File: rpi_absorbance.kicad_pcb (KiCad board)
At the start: 2 copper layers, 39 parts, among them CON1 BARREL_JACK, P1 DEVICE_CONN, P3 RPI_HEADER, P4 STEPPER_CONN, P5 SWITCH_CONN, Q1 NPN, U1 R-78B5.0-1.5L, U2 MEE1S1212SC, U3 DRV8825, U4 TCA9406DCUR

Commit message: Revise circuit
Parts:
- C13: footprint Capacitors_SMD:c_elec_8x6.7 -> Capacitors_SMD:C_1206
- moved Q1 41.0 mm to (157.2, 119.1)
- moved U2 39.8 mm to (155.4, 114.2)
- moved C7 14.6 mm to (112.5, 116.3)
- moved C10 14.6 mm to (115.7, 102.6)
- moved C14 14.6 mm to (115.7, 102.6)
- moved C15 14.6 mm to (115.7, 102.6)
- moved C16 14.6 mm to (115.7, 102.6)
- moved C17 14.6 mm to (115.7, 102.6)
- moved C18 14.6 mm to (115.7, 102.6)
- moved C4 14.6 mm to (107.2, 119.2)
- moved C8 14.6 mm to (115.7, 102.6)
- moved C9 14.6 mm to (115.7, 102.6)
- moved R10 14.6 mm to (115.7, 102.6)
- moved R2 14.6 mm to (115.7, 102.6)
- moved R3 14.6 mm to (115.7, 102.6)
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
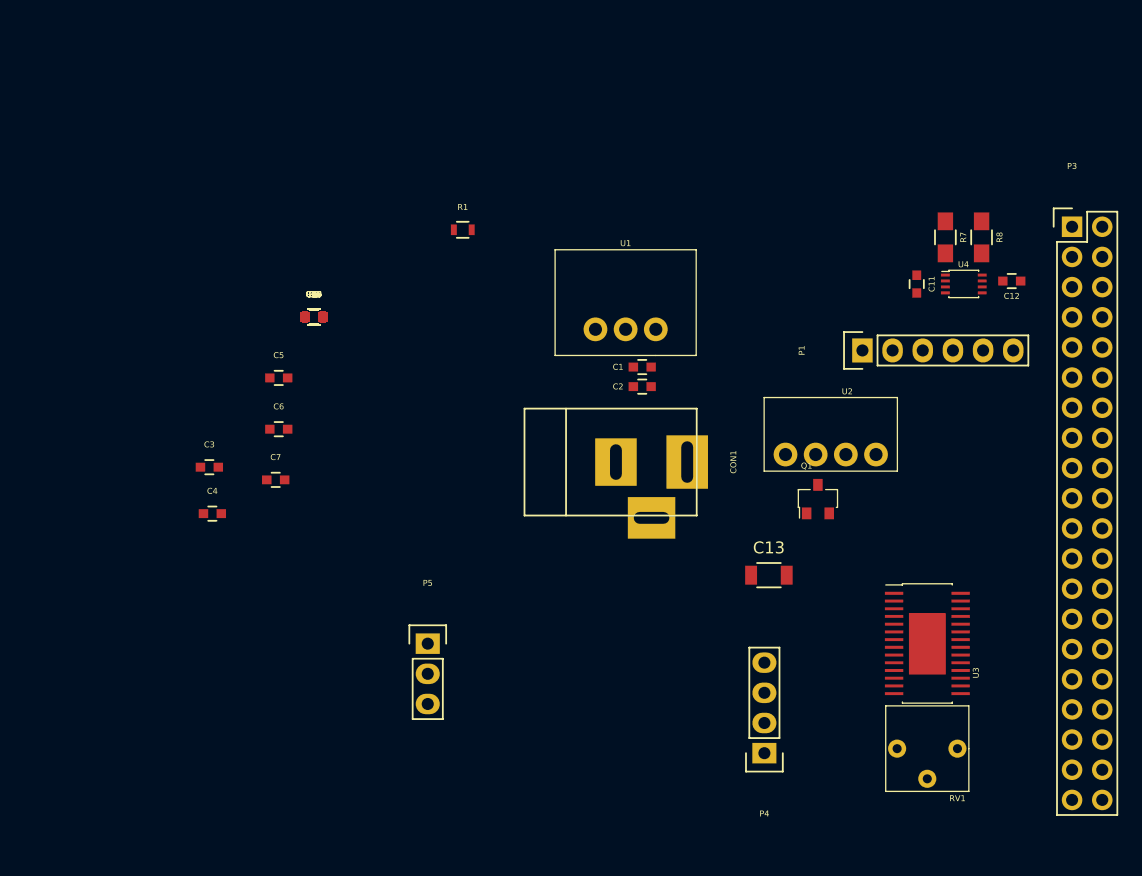
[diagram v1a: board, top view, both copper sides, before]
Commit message: Update footprints
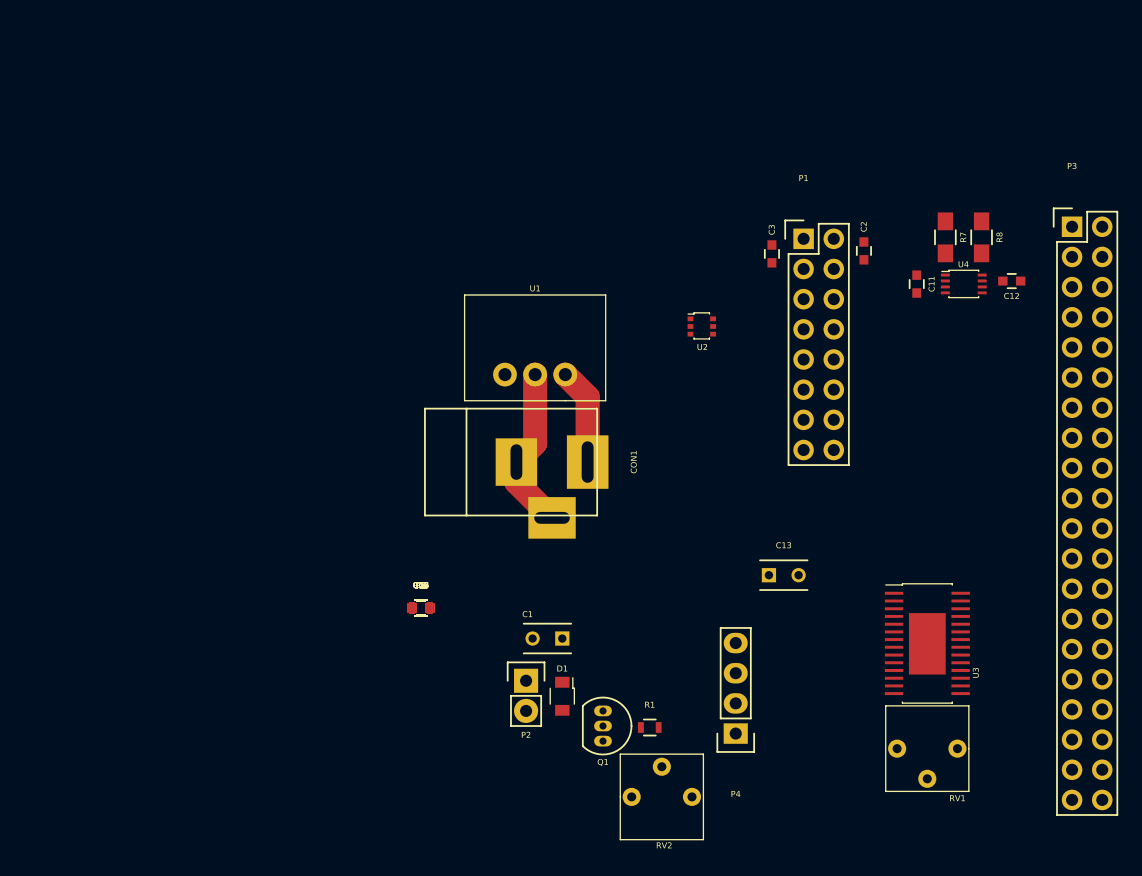
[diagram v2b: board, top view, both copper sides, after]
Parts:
- removed C10, C7, C8, C9: .1u, Capacitors_SMD:C_0603
- removed C4, C5, C6: 10u, Capacitors_SMD:C_0603
- removed P5: SWITCH_CONN, Pin_Headers:Pin_Header_Straight_1x03
- added D1: D, footprints:SOD-123, F.Cu at (136.7, 133.3)
- added P2: CONN_01X02, Pin_Headers:Pin_Header_Straight_1x02, F.Cu at (133.6, 133.2)
- added RV2: POT, footprints:BOURNS_3362P, F.Cu at (142.5, 143.0)
- C1: value .1u -> 100u; footprint Capacitors_SMD:C_0603 -> Capacitors_ThroughHole:C_Rect_L4_W2.5_P2.5
- C13: footprint Capacitors_SMD:C_1206 -> Capacitors_ThroughHole:C_Rect_L4_W2.5_P2.5
- P1: value DEVICE_CONN -> CONN_02X08; footprint Pin_Headers:Pin_Header_Straight_1x06 -> Pin_Headers:Pin_Header_Straight_2x08
- Q1: value NPN -> ZTX692B; footprint footprints:3-CP -> TO_SOT_Packages_THT:TO-92_Inline_Narrow_Oval
- R1: value 500 -> 1k
- U2: value MEE1S1212SC -> MUN5216DW1T1G; footprint footprints:MEE1-4-SIP -> footprints:SOT−363
- moved C3 50.7 mm to (154.3, 97.3), turned to 270 degrees
- moved R1 44.8 mm to (144.0, 137.2)
- moved C14 26.1 mm to (124.8, 127.1)
- moved C15 26.1 mm to (124.8, 127.1)
- moved C16 26.1 mm to (124.8, 127.1)
- moved C17 26.1 mm to (124.8, 127.1)
- moved C18 26.1 mm to (124.8, 127.1)
- moved R10 26.1 mm to (124.8, 127.1)
- moved R2 26.1 mm to (124.8, 127.1)
- moved R3 26.1 mm to (124.8, 127.1)
- moved R4 26.1 mm to (124.8, 127.1)
- moved R5 26.1 mm to (124.8, 127.1)
- moved R6 26.1 mm to (124.8, 127.1)
- moved R9 26.1 mm to (124.8, 127.1)
- moved Q1 23.9 mm to (140.1, 135.8), turned to 270 degrees
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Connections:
- C2 pad 1: +12V -> +5V
- C3 pad 1: +12V -> GND
- C3 pad 2: GND -> +12V
- CON1 pad 3: (no net) -> GND
- P1 pad 2: +5V -> GND
- P1 pad 3: /5vSDA -> +12V
- P1 pad 4: /5vSCL -> +5V
- P1 pad 5: /ISO-0v -> Net-(P1-Pad5)
- P1 pad 6: /ISO-12v -> /5vSDA
- P3 pad 11: /MODE2 -> /LED2
- P3 pad 13: /MODE1 -> /SWITCH1
- P3 pad 15: /MODE0 -> /SWITCH2
- P3 pad 19: /STEP -> /GPIO10
- P3 pad 21: /nENBL -> /GPIO9
- P3 pad 23: /DIR -> /GPIO11
- P3 pad 24: (no net) -> /PERI
- P3 pad 26: (no net) -> /nSLEEP
- P3 pad 29: /DECAY -> /MODE2
- P3 pad 31: /nFAULT -> /MODE1
- P3 pad 32: (no net) -> /nRESET
- P3 pad 33: /nSLEEP -> /MODE0
- P3 pad 35: /nRESET -> /STEP
- P3 pad 36: (no net) -> /nFAULT
- P3 pad 37: /SWITCH1 -> /nENBL
- P3 pad 38: (no net) -> /DECAY
- P3 pad 40: /SWITCH2 -> /DIR
- P3 pad 7: /LED_CTRL -> /LED1
- Q1 pad 1: Net-(Q1-Pad1) -> Net-(D1-Pad2)
- Q1 pad 2: GND -> Net-(Q1-Pad2)
- Q1 pad 3: Net-(Q1-Pad3) -> GND
- R1 pad 1: /LED_CTRL -> Net-(Q1-Pad2)
- R1 pad 2: Net-(Q1-Pad1) -> Net-(R1-Pad2)
- U2 pad 1: Net-(Q1-Pad3) -> GND
- U2 pad 2: +12V -> /LED1
- U2 pad 3: /ISO-0v -> Net-(P1-Pad7)
- U2 pad 4: /ISO-12v -> GND
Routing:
- net GND: track 0.00 -> 14.0 mm
- net +12V: track 0.00 -> 8.15 mm

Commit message: Update layout
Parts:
- moved C17 38.2 mm to (162.9, 125.1), turned to 90 degrees
- moved C16 36.9 mm to (161.7, 126.7), turned to 270 degrees
- moved R2 35.4 mm to (160.1, 126.7), turned to 270 degrees
- moved R4 35.4 mm to (159.9, 131.1), turned to 180 degrees
- moved R3 35.2 mm to (159.9, 129.0), turned to 180 degrees
- moved C15 34.4 mm to (158.6, 133.3), turned to 90 degrees
- moved C14 33.9 mm to (158.6, 126.7), turned to 270 degrees
- moved C18 27.6 mm to (152.1, 123.3)
- moved R10 27.6 mm to (152.1, 123.3)
- moved R5 27.6 mm to (152.1, 123.3)
- moved R6 27.6 mm to (152.1, 123.3)
- moved R9 27.6 mm to (152.1, 123.3)
- moved P4 9.78 mm to (161.0, 137.4), turned to 270 degrees
- moved RV1 5.08 mm to (164.8, 139.1), turned to 0 degrees
- moved C13 4.07 mm to (151.5, 127.5), turned to 270 degrees
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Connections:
- RV2 pad 1: /PERI -> GND
- RV2 pad 3: GND -> /PERI
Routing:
- net +12V: track 8.15 -> 25.9 mm
- net Net-(R3-Pad1): track 0.00 -> 3.98 mm
- net Net-(R4-Pad1): track 0.00 -> 3.95 mm
- net Net-(C16-Pad1): track 0.00 -> 3.40 mm
- net /BOUT2: track 0.00 -> 3.18 mm, vias 0 -> 2
- net /AOUT2: track 0.00 -> 2.60 mm, vias 0 -> 2
- net GND: track 14.0 -> 16.4 mm, vias 0 -> 1
- net /AOUT1: track 0.00 -> 2.32 mm, vias 0 -> 2
- net /BOUT1: track 0.00 -> 2.31 mm, vias 0 -> 2
- net Net-(C17-Pad2): track 0.00 -> 2.28 mm
- net Net-(C17-Pad1): track 0.00 -> 1.93 mm
- net Net-(RV1-Pad2): track 0.00 -> 0.65 mm

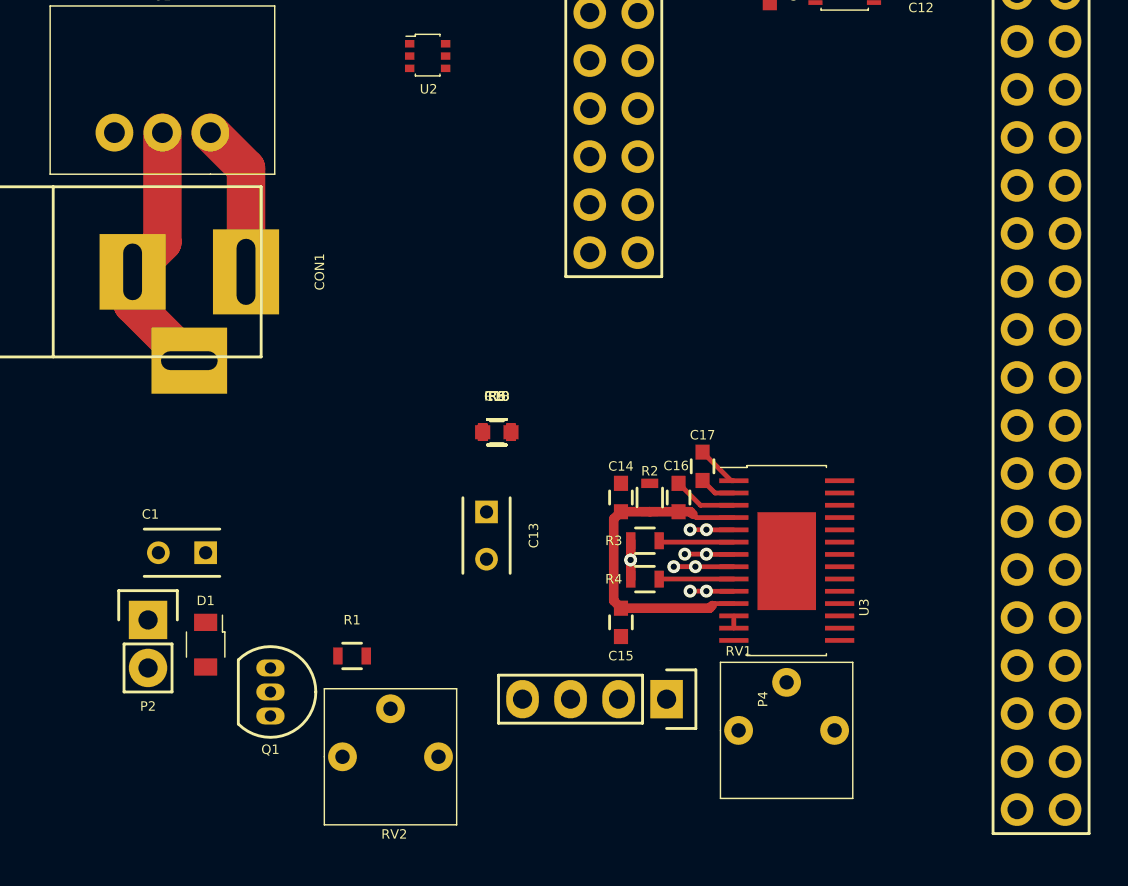
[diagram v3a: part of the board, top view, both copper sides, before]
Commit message: Complete stepper driver circuit
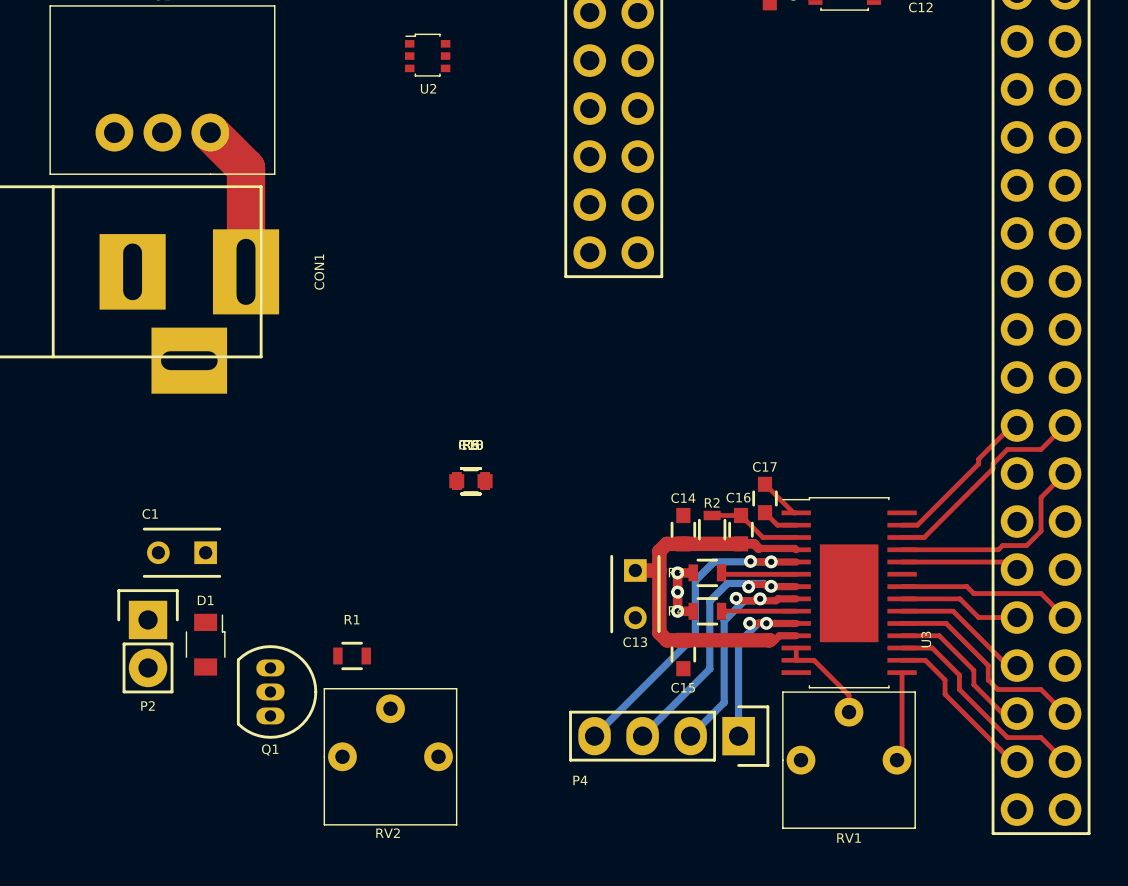
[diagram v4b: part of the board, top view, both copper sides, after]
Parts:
- moved C13 8.46 mm to (159.4, 130.6)
- moved P4 4.28 mm to (164.8, 139.4)
- moved C14 3.71 mm to (161.9, 128.4)
- moved C16 3.71 mm to (165.0, 128.4)
- moved R2 3.71 mm to (163.4, 128.4)
- moved C15 3.71 mm to (161.9, 135.1)
- moved R4 3.71 mm to (163.2, 132.8)
- moved C17 3.71 mm to (166.2, 126.8)
- moved U3 3.71 mm to (167.9, 127.6)
- moved R3 3.71 mm to (163.2, 130.7)
- moved RV1 3.66 mm to (168.1, 140.6)
- moved C18 2.93 mm to (150.7, 125.9)
- moved R10 2.93 mm to (150.7, 125.9)
- moved R5 2.93 mm to (150.7, 125.9)
- moved R6 2.93 mm to (150.7, 125.9)
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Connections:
- P1 pad 16: /GPIO11 -> (no net)
- P3 pad 23: /GPIO11 -> /nHOME
- P3 pad 24: /PERI -> /MODE2
- P3 pad 26: /nSLEEP -> /MODE1
- P3 pad 29: /MODE2 -> /MODE0
- P3 pad 31: /MODE1 -> /nENBL
- P3 pad 32: /nRESET -> /STEP
- P3 pad 33: /MODE0 -> /DIR
- P3 pad 35: /STEP -> /nFAULT
- P3 pad 36: /nFAULT -> /DECAY
- P3 pad 37: /nENBL -> /nRESET
- P3 pad 38: /DECAY -> /nSLEEP
- P3 pad 40: /DIR -> /PERI
- RV1 pad 1: /V3P3 -> GND
- RV1 pad 3: GND -> /V3P3
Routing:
- net /AOUT1: track 2.32 -> 17.3 mm
- net /AOUT2: track 2.60 -> 14.7 mm
- net GND: track 16.4 -> 4.71 mm, vias 1 -> 3
- net /nSLEEP: track 0.00 -> 11.6 mm
- net /MODE1: track 0.00 -> 11.3 mm
- net /MODE2: track 0.00 -> 11.2 mm
- net /DECAY: track 0.00 -> 11.0 mm
- net /STEP: track 0.00 -> 9.30 mm
- net /BOUT2: track 3.18 -> 12.3 mm
- net /nRESET: track 0.00 -> 8.75 mm
- net /nHOME: track 0.00 -> 8.42 mm
- net /nFAULT: track 0.00 -> 8.24 mm
- net /DIR: track 0.00 -> 7.28 mm
- net /BOUT1: track 2.31 -> 9.30 mm
- net /nENBL: track 0.00 -> 6.49 mm
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
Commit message: Reorganize pcb
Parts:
- moved R5 24.6 mm to (175.3, 127.4), turned to 270 degrees
- moved D1 17.7 mm to (152.7, 125.7)
- moved P2 17.1 mm to (148.8, 125.5)
- moved C1 14.6 mm to (148.8, 121.7), turned to 0 degrees
- moved U2 14.6 mm to (158.4, 112.4)
- moved CON1 13.3 mm to (145.3, 110.7)
- moved U1 13.3 mm to (149.6, 103.4)
- moved Q1 13.3 mm to (152.7, 131.6), turned to 0 degrees
- moved C2 13.1 mm to (170.9, 106.7)
- moved P1 12.9 mm to (165.9, 105.4)
- moved C3 12.8 mm to (163.1, 106.7)
- moved C11 9.99 mm to (176.3, 101.9), turned to 0 degrees
- moved R1 9.54 mm to (153.9, 135.6), turned to 270 degrees
- moved U4 6.73 mm to (175.5, 100.3), turned to 0 degrees
- moved C18 6.37 mm to (156.5, 123.3)
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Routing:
- net +3V3: track 0.00 -> 5.98 mm
- net /3.3vSCL: track 0.00 -> 4.04 mm, vias 0 -> 1
- net /3.3vSDA: track 0.00 -> 3.86 mm
- net GND: track 4.71 -> 6.43 mm
- net +5V: track 0.00 -> 1.47 mm
- net /MODE2: track 11.2 -> 12.0 mm
- net /nHOME: track 8.42 -> 9.16 mm

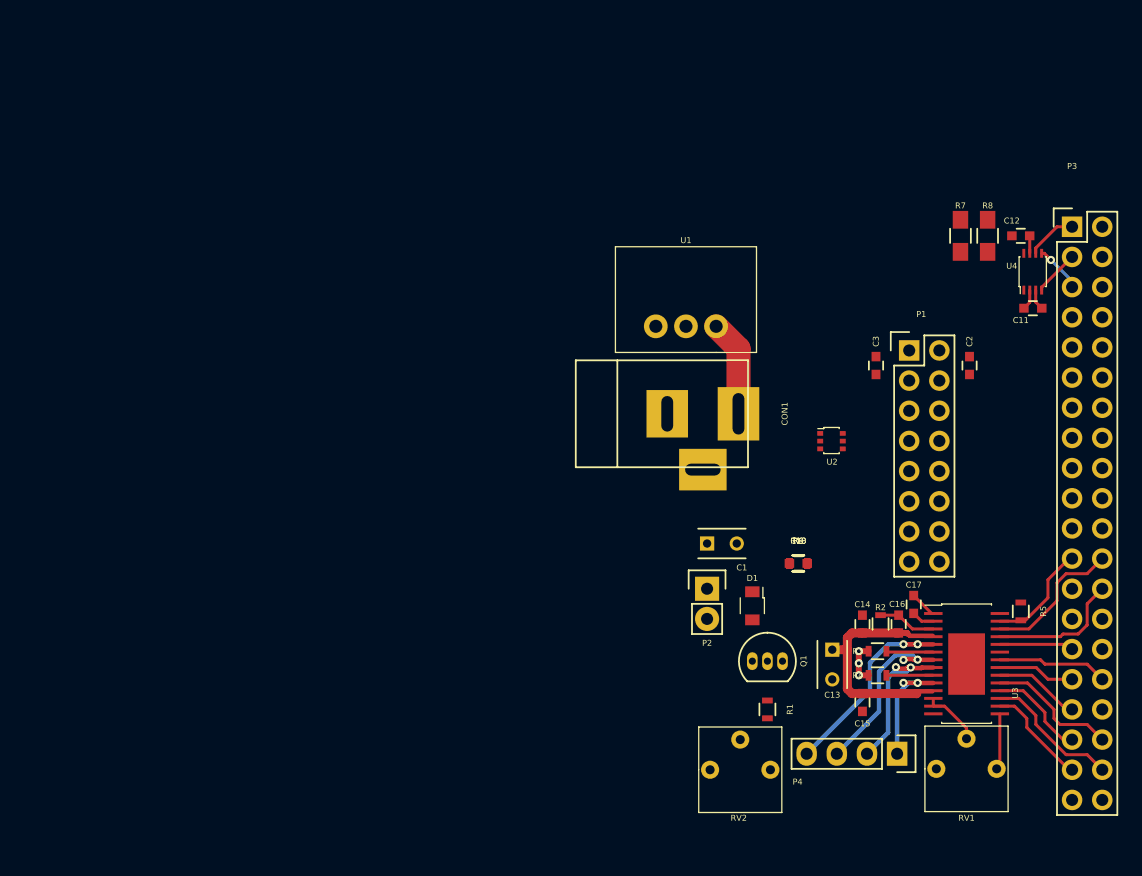
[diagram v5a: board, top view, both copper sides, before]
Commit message: Change potentiometer footprint
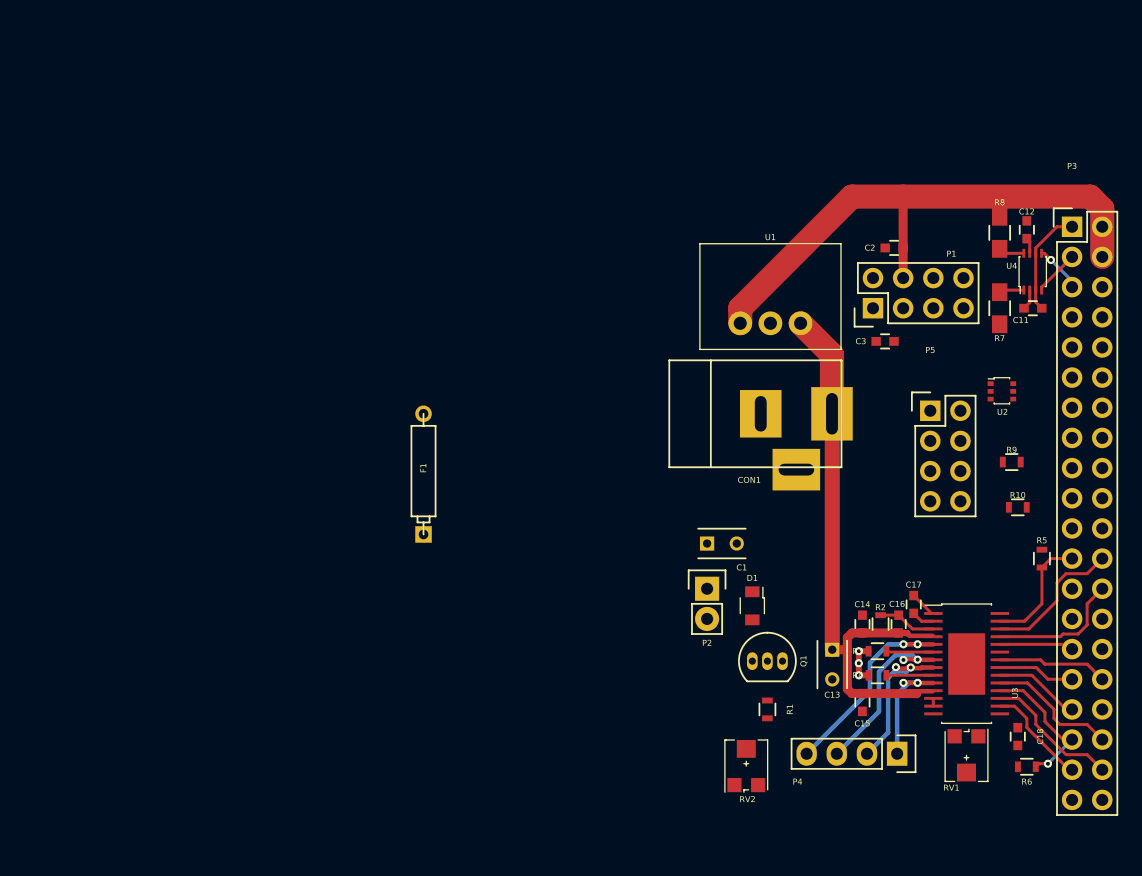
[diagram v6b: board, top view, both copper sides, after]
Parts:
- added F1: F_Small, Discret:CP4, F.Cu at (125.0, 115.8)
- added P5: CONN_02X04, Pin_Headers:Pin_Header_Straight_2x04, F.Cu at (167.6, 110.5)
- P1: value CONN_02X08 -> CONN_02X04; footprint Pin_Headers:Pin_Header_Straight_2x08 -> Pin_Headers:Pin_Header_Straight_2x04
- RV1, RV2: footprint footprints:BOURNS_3362P -> footprints:BOURNS_TC33
- moved R6 25.8 mm to (175.8, 140.5)
- moved C18 23.5 mm to (175.0, 137.9), turned to 270 degrees
- moved R9 19.9 mm to (174.5, 114.8)
- moved R10 19.1 mm to (175.0, 118.6)
- moved U2 15.0 mm to (172.7, 108.2)
- moved C2 11.8 mm to (164.6, 96.8), turned to 180 degrees
- moved CON1 7.87 mm to (153.2, 110.7)
- moved U1 7.12 mm to (156.7, 103.1)
- moved R7 6.93 mm to (173.5, 101.9), turned to 90 degrees
- moved R5 4.79 mm to (177.0, 122.9)
- moved P1 4.68 mm to (162.8, 101.9), turned to 90 degrees
- moved RV2 3.09 mm to (152.1, 140.2)
- moved RV1 2.71 mm to (170.7, 139.7), turned to 180 degrees
- moved C3 2.17 mm to (163.8, 104.6), turned to 0 degrees
- moved R8 1.05 mm to (173.5, 95.5)
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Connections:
- C3 pad 2: +12V -> Net-(C3-Pad2)
- P1 pad 3: +12V -> Net-(C3-Pad2)
- R5 pad 1: /V3P3 -> +3V3
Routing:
- net +5V: track 1.47 -> 49.8 mm
- net +12V: track 28.7 -> 49.2 mm
- net /V3P3: track 4.74 -> 0.00 mm
- net Net-(RV1-Pad2): track 5.10 -> 0.65 mm
- net /nFAULT: track 8.24 -> 12.5 mm, vias 0 -> 1
- net +3V3: track 5.98 -> 9.08 mm
- net /5vSDA: track 0.00 -> 2.46 mm
- net /5vSCL: track 0.17 -> 1.66 mm
- net /nHOME: track 9.16 -> 10.1 mm
